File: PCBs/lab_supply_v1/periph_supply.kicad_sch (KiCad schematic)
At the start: 15 parts, among them J2 USB_C_Receptacle_USB2.0_16P, J3 USB_A, J4 USB_A, U12 LMR14050SDDAR

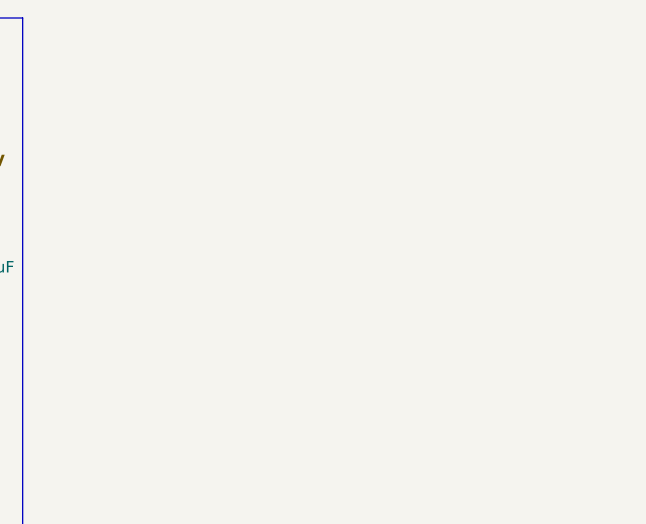
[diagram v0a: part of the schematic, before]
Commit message: Updated PCB, FTDI interface
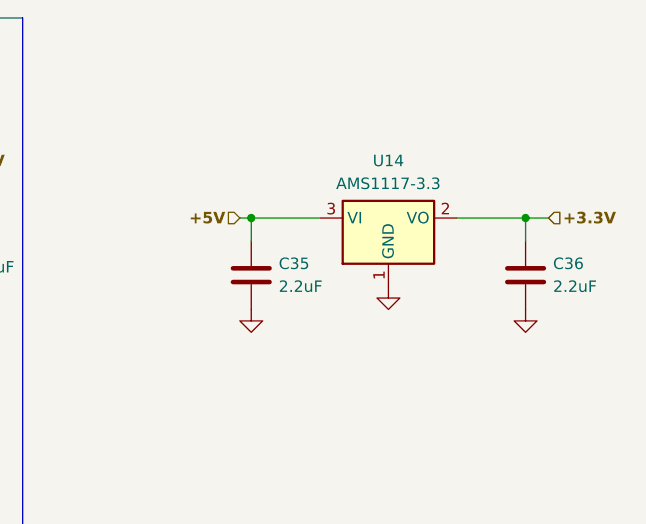
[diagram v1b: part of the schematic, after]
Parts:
- added C35, C36: 2.2uF, symbol Device:C
- added U14: AMS1117-3.3, Package_TO_SOT_SMD:SOT-223-3_TabPin2, symbol Regulator_Linear:AMS1117-3.3
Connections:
- net +5V: now also C35.1, U14.3 (VI)
- net GND: now also C35.2, C36.2, U14.1 (GND)
- new net +3.3V: C36.1, U14.2 (VO)

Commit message: Updated PCB added current sense buffer added ADC/DAC for current/voltage sensing added ACDC converter bypass made optimal supply voltage 36 V @ 5 A
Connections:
- net +32V renamed +36V
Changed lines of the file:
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@@
-		)
-	)
-	(hierarchical_label "+32V"
-		(shape input)
-		(at 20.32 26.67 180)
-		(fields_autoplaced yes)
-		(effects
-			(font
-				(size 1.27 1.27)
-				(bold yes)
-			)
-			(justify right)
 		)
 	)
@@
 		)
 	)
+	(hierarchical_label "+36V"
+		(shape input)
+		(at 20.32 26.67 180)
+		(fields_autoplaced yes)
+		(effects
+			(font
+				(size 1.27 1.27)
+			)
+			(justify right)
+		)
+	)
